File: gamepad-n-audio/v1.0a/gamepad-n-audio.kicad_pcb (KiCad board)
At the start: 2 copper layers, 40 x 20 mm, 36 parts, among them J1 5V, J2 Switchcraft_35RAPC4BHN3, J3 Gamepads, J4 PMOD, J5 jmp, U1 74LVC2T45, U2 74LVC2T45, U3 74LVC2T45, U4 74AUP2G3404, U5 74AUP2G3404

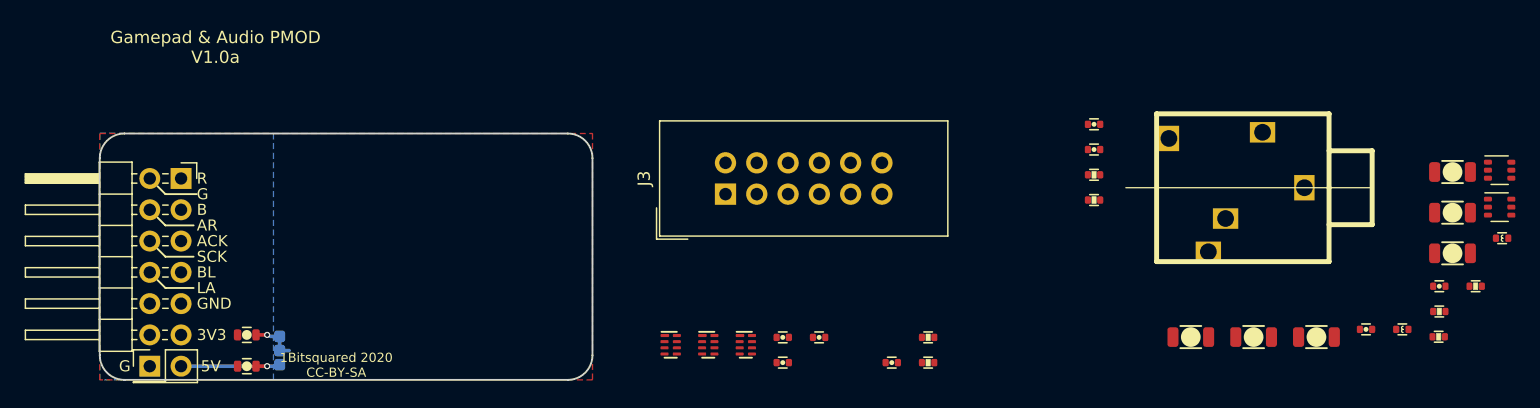
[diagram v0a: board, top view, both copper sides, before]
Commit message: Finished first routing pass on the gamepad & audio Pmod.
This is the status of the board after the Twitch stream on April 16th.
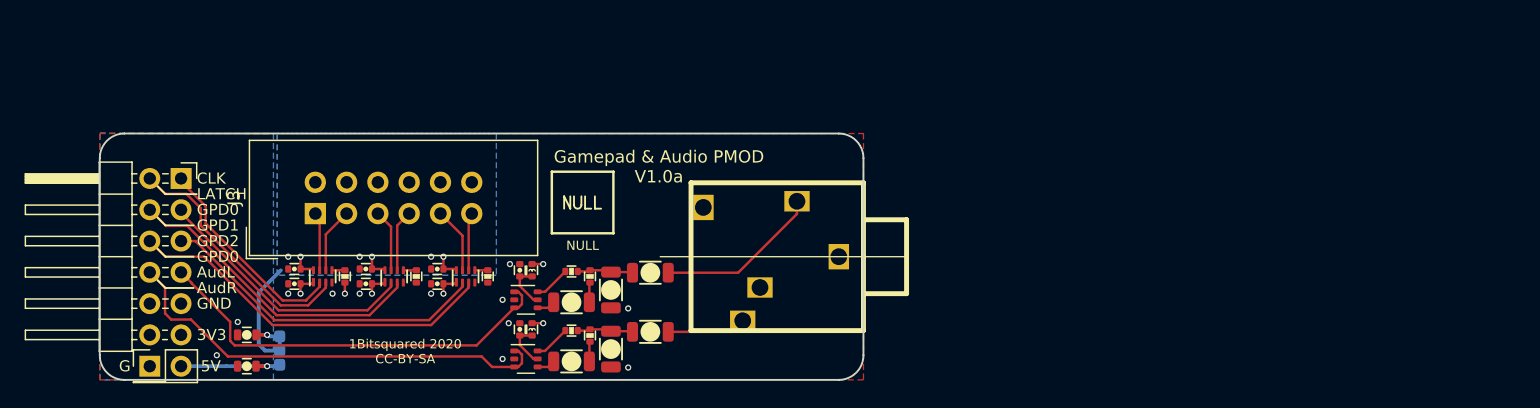
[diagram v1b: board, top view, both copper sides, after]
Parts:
- added REF**: null_Logo_SilkS_5mm, pkl_logos:null_Logo_SilkS_5mm, F.Cu at (76.6, 39.6)
- R4, R5, R6, R7: value 3k3 -> 1k
- moved U5 80.0 mm to (72.0, 52.3)
- moved U4 79.7 mm to (72.0, 47.5)
- moved FB1 78.8 mm to (72.5, 45.1), turned to 270 degrees
- moved C15 74.7 mm to (71.5, 49.9), turned to 90 degrees
- moved C16 72.3 mm to (75.7, 47.7), turned to 180 degrees
- moved R6 71.9 mm to (77.2, 45.6), turned to 270 degrees
- moved FB2 70.7 mm to (72.5, 49.9), turned to 270 degrees
- moved R5 70.5 mm to (75.7, 45.2), turned to 180 degrees
- moved R7 68.9 mm to (77.2, 50.4), turned to 270 degrees
- moved C9 68.9 mm to (71.5, 45.1), turned to 90 degrees
- moved C18 68.6 mm to (78.9, 46.7), turned to 270 degrees
- moved C20 65.1 mm to (82.1, 45.3)
- moved R1 61.4 mm to (57.3, 45.6), turned to 270 degrees
- moved C4 60.5 mm to (59.0, 46.2), turned to 180 degrees
- moved C17 55.4 mm to (75.7, 52.5), turned to 180 degrees
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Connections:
- C3 pad 2: Net-(C3-Pad2) -> GND
- C4 pad 2: Net-(C3-Pad2) -> GND
- C5 pad 1: Net-(C5-Pad1) -> +3V3
- C5 pad 2: Net-(C3-Pad2) -> GND
- J4 pad 10: /AudioL -> /AudioR
- J4 pad 4: /AudioR -> /AudioL
- U3 pad 1: Net-(C5-Pad1) -> +3V3
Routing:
- net /AudioR: track 0.50 -> 36.2 mm
- net /AudioL: track 0.00 -> 34.4 mm
- net /GPD3: track 0.00 -> 30.4 mm
- net /GPD2: track 0.00 -> 27.0 mm
- net /GPD1: track 0.00 -> 25.0 mm
- net /GPD0: track 0.00 -> 21.7 mm
- net /LATCH: track 0.00 -> 20.4 mm
- net /CLK: track 0.00 -> 17.1 mm
- net /xTVCC: track 0.76 -> 14.9 mm, vias 0 -> 3
- net Net-(C20-Pad2): track 0.00 -> 13.5 mm
- net +3V3: track 1.66 -> 10.4 mm, vias 1 -> 7
- net Net-(C19-Pad2): track 0.00 -> 6.42 mm
- net /xGPD2: track 0.00 -> 5.34 mm
- net /xLATCH: track 0.00 -> 5.30 mm
- net /xGPD0: track 0.00 -> 5.04 mm
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- added copper zone on In2.Cu, net +3V3
- added copper zone on B.Cu, net /xTVCC
- added copper zone on In2.Cu, net /xTVCC
- added copper zone on In1.Cu, net GND
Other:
- board size 40 x 20 mm -> 62 x 20 mm
- copper layers 2 -> 4
- board text added: "AuL"
- board text added: "AuR"
- board text added: "AudL"
- board text added: "AudR"
- board text added: "CLK"
- board text added: "GD1"
- board text added: "GD3"
- board text added: "GPD0"
- board text added: "GPD1"
- board text added: "GPD2"
- board text added: "LAT"
- board text added: "LATCH"
- board text removed: "ACK"
- board text removed: "AR"
- board text removed: "B"
- board text removed: "BL"
- board text removed: "LA"
- board text removed: "R"
- board text removed: "SCK"

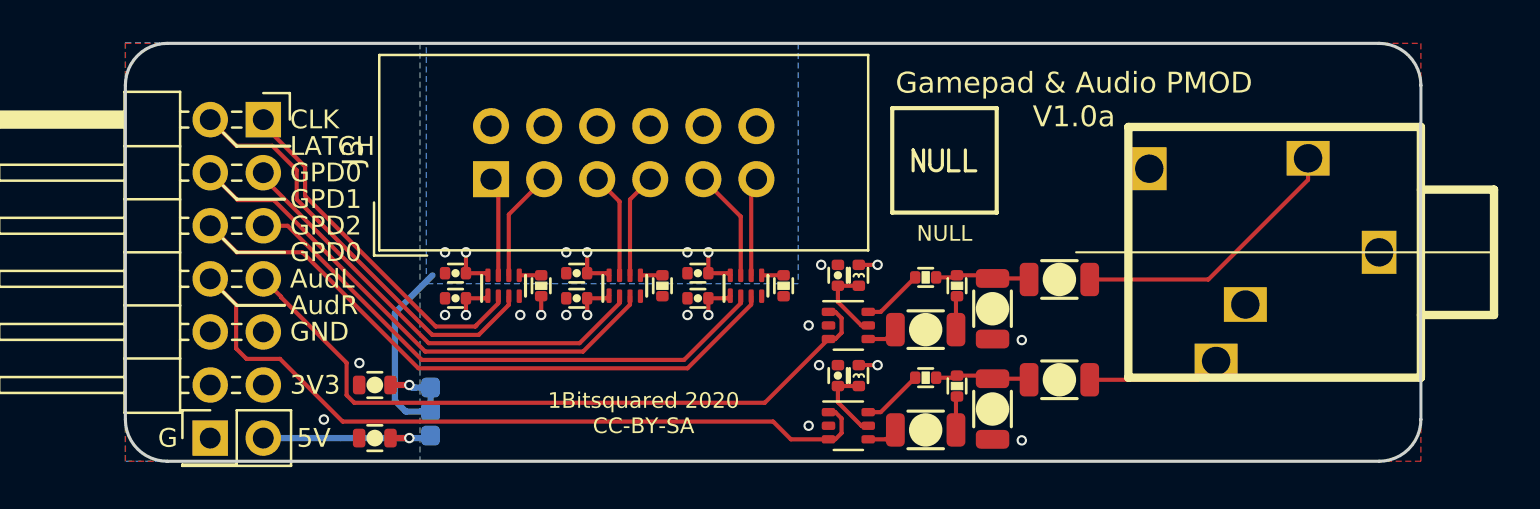
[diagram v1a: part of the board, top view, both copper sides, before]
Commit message: Compression pass on the gamepad & audio Pmod.
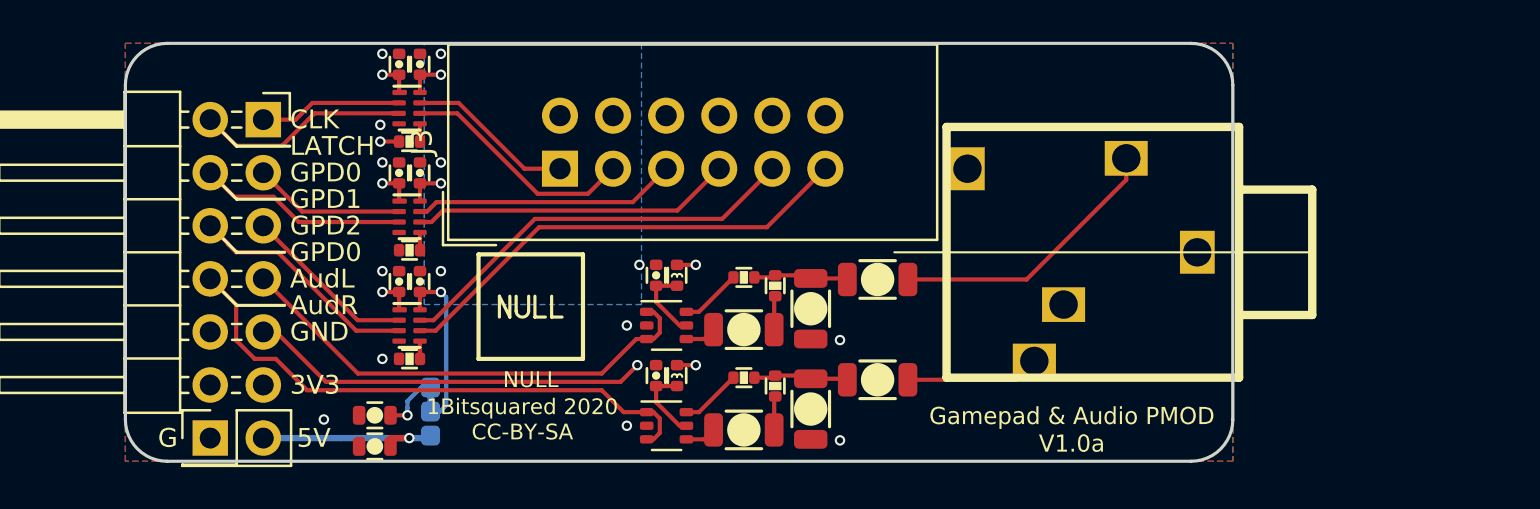
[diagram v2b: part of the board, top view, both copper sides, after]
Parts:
- moved REF** 21.0 mm to (56.8, 46.6)
- moved R3 18.2 mm to (51.0, 49.1), turned to 180 degrees
- moved U3 16.2 mm to (51.0, 47.5), turned to 0 degrees
- moved C5 14.3 mm to (50.5, 45.4), turned to 90 degrees
- moved C8 13.3 mm to (51.5, 45.4), turned to 90 degrees
- moved R2 12.2 mm to (51.0, 43.9), turned to 180 degrees
- moved C3 11.5 mm to (50.5, 35.0), turned to 90 degrees
- moved U2 10.8 mm to (51.0, 42.3), turned to 0 degrees
- moved C4 10.4 mm to (50.5, 40.2), turned to 90 degrees
- moved C6 10.1 mm to (51.5, 35.0), turned to 90 degrees
- moved U1 9.62 mm to (51.0, 37.1), turned to 0 degrees
- moved R1 9.34 mm to (51.0, 38.7), turned to 180 degrees
- moved C7 8.90 mm to (51.5, 40.2), turned to 90 degrees
- moved C14 8.70 mm to (70.2, 51.5)
- moved C15 8.70 mm to (62.8, 49.9)
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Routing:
- net /GPD3: track 30.4 -> 11.1 mm
- net GND: track 0.00 -> 19.2 mm
- net /GPD2: track 27.0 -> 8.37 mm
- net /xGPD3: track 4.70 -> 22.6 mm
- net /GPD1: track 25.0 -> 10.0 mm
- net /xGPD2: track 5.34 -> 19.9 mm
- net /GPD0: track 21.7 -> 7.27 mm
- net /AudioL: track 34.4 -> 23.6 mm
- net /xGPD1: track 5.00 -> 15.4 mm
- net /CLK: track 17.1 -> 6.83 mm
- net /LATCH: track 20.4 -> 10.2 mm
- net /AudioR: track 36.2 -> 26.7 mm
- net /xGPD0: track 5.04 -> 12.6 mm
- net /xLATCH: track 5.30 -> 11.3 mm
- net /xCLK: track 4.74 -> 8.00 mm
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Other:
- board size 62 x 20 mm -> 53 x 20 mm

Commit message: gpna: Updated BOM Keys and a few other details.
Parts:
- moved REF** 0.50 mm to (78.2, 45.8)
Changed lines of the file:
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@@
   )
   (module pkl_logos:null_Logo_SilkS_5mm locked (layer B.Cu)
-    (at 78.69361 45.794674)
+    (at 78.19361 45.794674)
+    (attr virtual)
     (fp_text reference REF** (at 0 -4) (layer B.Fab) hide
       (effects (font (size 1 1) (thickness 0.15)) (justify mirror))
@@
   (module pkl_logos:null_Logo_SilkS_5mm locked (layer F.Cu)
     (at 56.8 46.6)
+    (attr virtual)
     (fp_text reference REF** (at 0 4) (layer F.Fab) hide
       (effects (font (size 1 1) (thickness 0.15)))
@@
   (gr_line (start 61.276 53.652) (end 61.276 49.588) (layer B.SilkS) (width 0.15))
   (gr_line (start 61.276 49.588) (end 47.941 49.588) (layer B.SilkS) (width 0.15))
-  (gr_text NULL (at 78.89361 42.394674 180) (layer B.SilkS)
+  (gr_text NULL (at 78.39361 42.394674 180) (layer B.SilkS)
     (effects (font (size 0.75 0.75) (thickness 0.1875)) (justify mirror))
   )
